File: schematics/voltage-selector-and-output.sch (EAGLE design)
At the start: 30 parts, among them IC1 5V, IC2 MIC2941, IC3 MCP41010P, IC5 12V, IC6 ATTINY85, Q1 2N3906

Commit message: Updated the schematics
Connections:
- net PB4: now also IC3./CS
- net PB5: no longer IC3./CS
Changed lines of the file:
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@@
 <label x="-5.08" y="172.72" size="1.778" layer="95"/>
-</segment>
-<segment>
-<pinref part="IC3" gate="P1" pin="/CS"/>
-<wire x1="43.18" y1="144.78" x2="45.72" y2="144.78" width="0.1524" layer="91"/>
-<label x="45.72" y="144.78" size="1.778" layer="95"/>
 </segment>
 </net>
@@
 <label x="-25.4" y="129.54" size="1.778" layer="95"/>
 </segment>
+<segment>
+<pinref part="IC3" gate="P1" pin="/CS"/>
+<wire x1="43.18" y1="144.78" x2="45.72" y2="144.78" width="0.1524" layer="91"/>
+<label x="45.72" y="144.78" size="1.778" layer="95"/>
+</segment>
 </net>

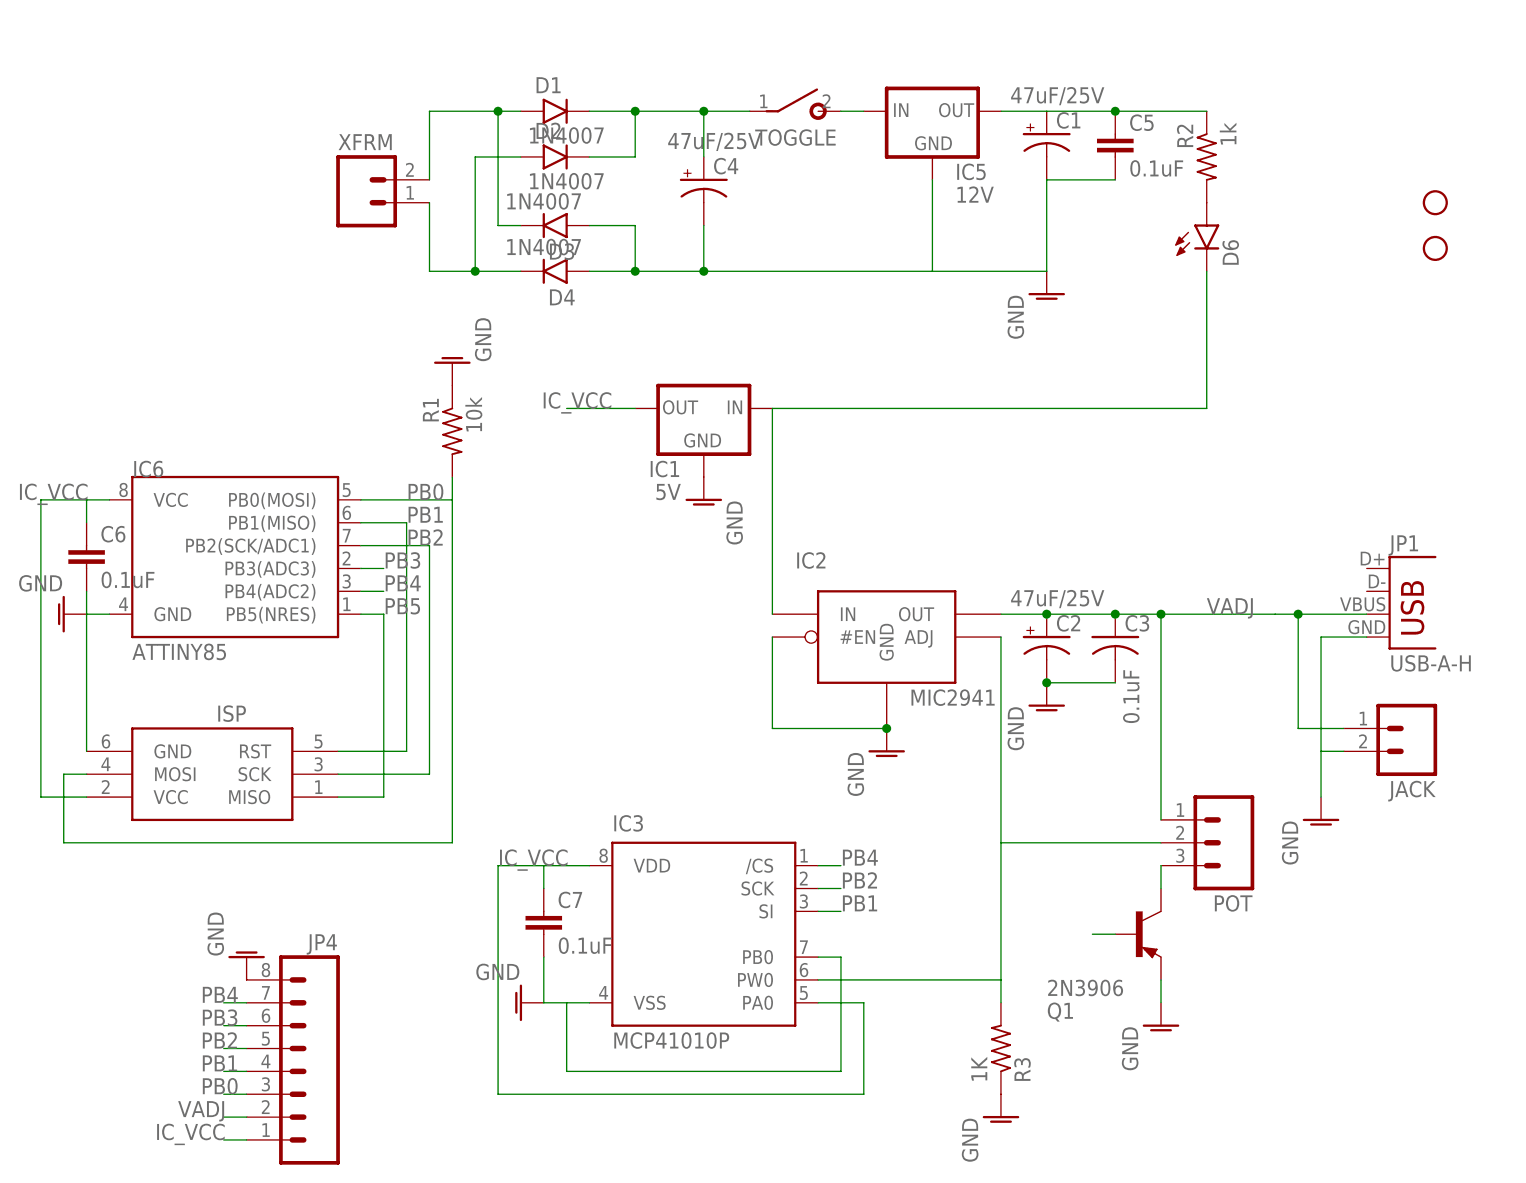
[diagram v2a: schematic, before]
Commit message: Decided to remove the "adjustable" option because it was kinda useless
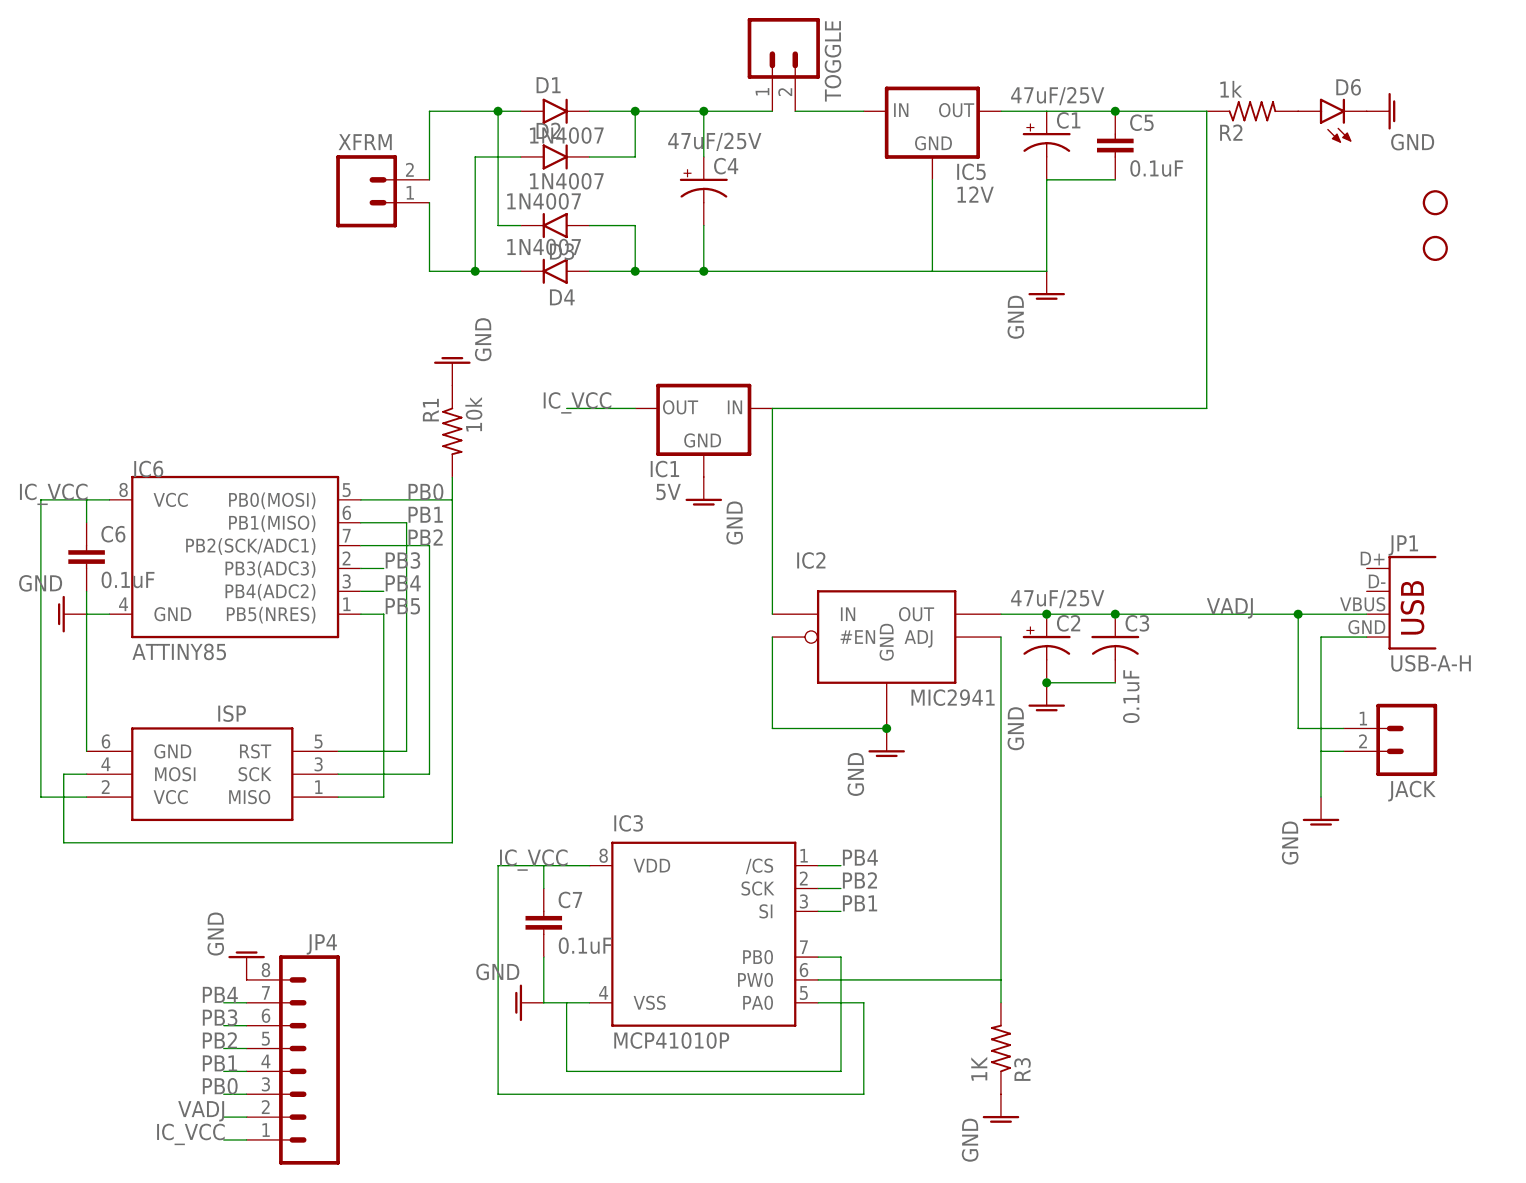
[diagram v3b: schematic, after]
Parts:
- removed POT: (no value), SparkFun:M03PTH
- removed Q1: 2N3906, transistor-pnp:2N3906
- TOGGLE: value SPST -> (none); device gm-switches:SPST -> SparkFun:M02PTH
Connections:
- removed net N$5: C1.+, C5.1, IC5.OUT, R2.1
- removed net N$6: POT.2
- removed net N$7: POT.3, Q1.C
- removed net N$8: Q1.B
- new net N$11: JACK.1
- net AGND: now also D6.C; no longer Q1.E
- net N$1: now also TOGGLE.2; no longer TOGGLE.S
- net N$9: now also TOGGLE.1; no longer TOGGLE.P
- net RECTIFIED_12VCC: now also C1.+, C5.1, IC5.OUT, R2.1; no longer D6.C
- net VADJ: no longer JACK.1, POT.1
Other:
- moved on the sheet: D6, R2
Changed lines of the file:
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@@
 <part name="IC1" library="v-reg" deviceset="78XXS" device="" value="5V"/>
 <part name="R1" library="rcl-ez" deviceset="R-US_" device="0207/5V" value="10k"/>
-<part name="POT" library="SparkFun" deviceset="M03" device="PTH"/>
-<part name="GND11" library="supply1" deviceset="AGND" device="" value="GND"/>
 <part name="IC3" library="microchip-custom" deviceset="MCP41010" device="P"/>
 <part name="ISP" library="adafruit" deviceset="AVRISP" device="-6"/>
@@
 <part name="GND6" library="supply1" deviceset="AGND" device="" value="GND"/>
 <part name="D1" library="gm-diodes" deviceset="1N400X" device=".3" value="1N4007"/>
-<part name="TOGGLE" library="gm-switches" deviceset="SPST" device=""/>
 <part name="D2" library="gm-diodes" deviceset="1N400X" device=".3" value="1N4007"/>
 <part name="GND" library="supply1" deviceset="AGND" device="" value="GND"/>
@@
 <part name="C5" library="SparkFun-Capacitors" deviceset="CAP" device="PTH" value="0.1uF"/>
 <part name="JACK" library="SparkFun" deviceset="M02" device="PTH"/>
-<part name="Q1" library="transistor-pnp" deviceset="2N3906" device=""/>
 <part name="C6" library="SparkFun-Capacitors" deviceset="CAP" device="PTH" value="0.1uF"/>
 <part name="C7" library="SparkFun-Capacitors" deviceset="CAP" device="PTH" value="0.1uF"/>
@@
 <part name="JP1" library="SparkFun-Connectors" deviceset="USB" device="-A-H"/>
 <part name="R2" library="rcl-ez" deviceset="R-US_" device="0207/5V" value="1k"/>
+<part name="TOGGLE" library="SparkFun" deviceset="M02" device="PTH"/>
+<part name="GND9" library="supply1" deviceset="AGND" device="" value="GND"/>
 </parts>
 <sheets>
@@
 <instance part="IC1" gate="1" x="30.48" y="195.58" rot="MR0"/>
 <instance part="R1" gate="G$1" x="2.54" y="193.04" rot="MR270"/>
-<instance part="POT" gate="G$1" x="88.9" y="147.32" rot="R180"/>
-<instance part="GND11" gate="VR1" x="81.28" y="127"/>
 <instance part="IC3" gate="P1" x="30.48" y="137.16"/>
 <instance part="ISP" gate="G$1" x="-22.86" y="154.94" rot="R180"/>
@@
 <instance part="GND6" gate="VR1" x="10.16" y="129.54" rot="R270"/>
 <instance part="D1" gate="1" x="15.24" y="228.6"/>
-<instance part="TOGGLE" gate="G$1" x="40.64" y="228.6" rot="R270"/>
 <instance part="D2" gate="1" x="15.24" y="223.52"/>
 <instance part="GND" gate="VR1" x="68.58" y="208.28"/>
@@
 </instance>
 <instance part="XFRM" gate="G$1" x="-7.62" y="218.44"/>
-<instance part="D6" gate="G$1" x="86.36" y="215.9"/>
+<instance part="D6" gate="G$1" x="99.06" y="228.6" rot="R90"/>
 <instance part="C5" gate="G$1" x="76.2" y="223.52"/>
 <instance part="JACK" gate="G$1" x="109.22" y="160.02" rot="R180"/>
-<instance part="Q1" gate="G$1" x="78.74" y="137.16" rot="MR180"/>
 <instance part="C6" gate="G$1" x="-38.1" y="177.8"/>
 <instance part="C7" gate="G$1" x="12.7" y="137.16"/>
@@
 <instance part="STANDOFF2" gate="G$1" x="111.76" y="213.36"/>
 <instance part="JP1" gate="G$1" x="106.68" y="170.18"/>
-<instance part="R2" gate="G$1" x="86.36" y="223.52" rot="MR270"/>
+<instance part="R2" gate="G$1" x="91.44" y="228.6" rot="MR180"/>
+<instance part="TOGGLE" gate="G$1" x="38.1" y="236.22" rot="R270"/>
+<instance part="GND9" gate="VR1" x="106.68" y="228.6" rot="R90"/>
 </instances>
 <busses>
@@
 <segment>
 <wire x1="68.58" y1="172.72" x2="76.2" y2="172.72" width="0.1524" layer="91"/>
-<wire x1="81.28" y1="172.72" x2="76.2" y2="172.72" width="0.1524" layer="91"/>
 <wire x1="63.5" y1="172.72" x2="68.58" y2="172.72" width="0.1524" layer="91"/>
-<wire x1="81.28" y1="149.86" x2="81.28" y2="172.72" width="0.1524" layer="91"/>
 <junction x="68.58" y="172.72"/>
 <junction x="76.2" y="172.72"/>
@@
 <pinref part="C3" gate="G$1" pin="1"/>
 <pinref part="IC2" gate="G$1" pin="OUT"/>
-<wire x1="81.28" y1="172.72" x2="93.98" y2="172.72" width="0.1524" layer="91"/>
-<wire x1="96.52" y1="172.72" x2="96.52" y2="160.02" width="0.1524" layer="91"/>
-<junction x="96.52" y="172.72"/>
-<junction x="81.28" y="172.72"/>
-<pinref part="POT" gate="G$1" pin="1"/>
-<pinref part="JACK" gate="G$1" pin="1"/>
-<wire x1="101.6" y1="160.02" x2="96.52" y2="160.02" width="0.1524" layer="91"/>
+<wire x1="76.2" y1="172.72" x2="104.14" y2="172.72" width="0.1524" layer="91"/>
 <label x="86.36" y="172.72" size="1.778" layer="95"/>
-<wire x1="104.14" y1="172.72" x2="93.98" y2="172.72" width="0.1524" layer="91"/>
 <pinref part="JP1" gate="G$1" pin="VBUS"/>
 </segment>
@@
 <pinref part="GND8" gate="VR1" pin="AGND"/>
 <pinref part="R1" gate="G$1" pin="1"/>
-</segment>
-<segment>
-<pinref part="GND11" gate="VR1" pin="AGND"/>
-<pinref part="Q1" gate="G$1" pin="E"/>
-<wire x1="81.28" y1="132.08" x2="81.28" y2="129.54" width="0.1524" layer="91"/>
 </segment>
 <segment>
@@
 <wire x1="55.88" y1="210.82" x2="68.58" y2="210.82" width="0.1524" layer="91"/>
 </segment>
+<segment>
+<pinref part="GND9" gate="VR1" pin="AGND"/>
+<pinref part="D6" gate="G$1" pin="C"/>
+</segment>
 </net>
 <net name="PB5" class="0">
@@
 <pinref part="IC1" gate="1" pin="IN"/>
 <wire x1="38.1" y1="195.58" x2="38.1" y2="172.72" width="0.1524" layer="91"/>
-<wire x1="86.36" y1="210.82" x2="86.36" y2="195.58" width="0.1524" layer="91"/>
 <wire x1="86.36" y1="195.58" x2="38.1" y2="195.58" width="0.1524" layer="91"/>
-<pinref part="D6" gate="G$1" pin="C"/>
+<pinref part="IC5" gate="1" pin="OUT"/>
+<pinref part="C1" gate="G$1" pin="+"/>
+<pinref part="R2" gate="G$1" pin="1"/>
+<wire x1="86.36" y1="228.6" x2="76.2" y2="228.6" width="0.1524" layer="91"/>
+<pinref part="C5" gate="G$1" pin="1"/>
+<junction x="76.2" y="228.6"/>
+<wire x1="76.2" y1="228.6" x2="68.58" y2="228.6" width="0.1524" layer="91"/>
+<wire x1="68.58" y1="228.6" x2="63.5" y2="228.6" width="0.1524" layer="91"/>
+<wire x1="86.36" y1="195.58" x2="86.36" y2="228.6" width="0.1524" layer="91"/>
 </segment>
 </net>
@@
 <segment>
 <pinref part="D1" gate="1" pin="C"/>
-<pinref part="TOGGLE" gate="G$1" pin="P"/>
 <wire x1="17.78" y1="228.6" x2="22.86" y2="228.6" width="0.1524" layer="91"/>
 <wire x1="22.86" y1="228.6" x2="30.48" y2="228.6" width="0.1524" layer="91"/>
 <pinref part="D2" gate="1" pin="C"/>
-<wire x1="30.48" y1="228.6" x2="35.56" y2="228.6" width="0.1524" layer="91"/>
+<wire x1="30.48" y1="228.6" x2="38.1" y2="228.6" width="0.1524" layer="91"/>
 <wire x1="17.78" y1="223.52" x2="22.86" y2="223.52" width="0.1524" layer="91"/>
 <wire x1="22.86" y1="223.52" x2="22.86" y2="228.6" width="0.1524" layer="91"/>
@@
 <wire x1="30.48" y1="223.52" x2="30.48" y2="228.6" width="0.1524" layer="91"/>
 <junction x="30.48" y="228.6"/>
+<pinref part="TOGGLE" gate="G$1" pin="1"/>
 </segment>
 </net>
@@
 <segment>
 <pinref part="IC5" gate="1" pin="IN"/>
-<pinref part="TOGGLE" gate="G$1" pin="S"/>
-<wire x1="48.26" y1="228.6" x2="45.72" y2="228.6" width="0.1524" layer="91"/>
-</segment>
-</net>
-<net name="N$6" class="0">
-<segment>
-<pinref part="POT" gate="G$1" pin="2"/>
-<wire x1="81.28" y1="147.32" x2="63.5" y2="147.32" width="0.1524" layer="91"/>
-</segment>
-</net>
-<net name="N$7" class="0">
-<segment>
-<pinref part="POT" gate="G$1" pin="3"/>
-<wire x1="81.28" y1="144.78" x2="81.28" y2="142.24" width="0.1524" layer="91"/>
-<pinref part="Q1" gate="G$1" pin="C"/>
-</segment>
-</net>
-<net name="N$8" class="0">
-<segment>
-<pinref part="Q1" gate="G$1" pin="B"/>
-<wire x1="76.2" y1="137.16" x2="73.66" y2="137.16" width="0.1524" layer="91"/>
-</segment>
-</net>
-<net name="N$5" class="0">
-<segment>
-<pinref part="IC5" gate="1" pin="OUT"/>
-<pinref part="C1" gate="G$1" pin="+"/>
-<pinref part="R2" gate="G$1" pin="1"/>
-<wire x1="86.36" y1="228.6" x2="76.2" y2="228.6" width="0.1524" layer="91"/>
-<pinref part="C5" gate="G$1" pin="1"/>
-<junction x="76.2" y="228.6"/>
-<wire x1="76.2" y1="228.6" x2="68.58" y2="228.6" width="0.1524" layer="91"/>
-<wire x1="68.58" y1="228.6" x2="63.5" y2="228.6" width="0.1524" layer="91"/>
+<pinref part="TOGGLE" gate="G$1" pin="2"/>
+<wire x1="48.26" y1="228.6" x2="40.64" y2="228.6" width="0.1524" layer="91"/>
 </segment>
 </net>
@@
 </segment>
 </net>
+<net name="N$11" class="0">
+<segment>
+<junction x="96.52" y="172.72"/>
+<wire x1="96.52" y1="172.72" x2="96.52" y2="160.02" width="0.1524" layer="91"/>
+<pinref part="JACK" gate="G$1" pin="1"/>
+<wire x1="101.6" y1="160.02" x2="96.52" y2="160.02" width="0.1524" layer="91"/>
+</segment>
+</net>
